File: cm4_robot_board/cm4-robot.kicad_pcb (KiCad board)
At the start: 4 copper layers, 118 x 117 mm, 195 parts, among them J1 1747981-1, J10 Conn_01x04, J11 Conn_01x03, J12 Conn_01x04, J13 CAN Interface, J14 Conn_01x03, J15 Conn_02x04_Odd_Even, J17 Conn_01x04, J18 Conn_01x04, J19 Conn_01x04, J2 CAN Interface, J20 Conn_01x04, J21 Conn_01x03, J22 Conn_01x04, J23 Conn_01x01, J24 Conn_01x01, J25 RJ45, J3 USB_C_Receptacle_USB2.0, J4 Conn_01x04, J5 Conn_01x04, J6 Conn_01x04, J7 USB_A, J8 HIGHCURRENTPAD2, J9 HIGHCURRENTPAD2, Q1 Q_PMOS_GSD, Q2 Q_NMOS_GSD, Q3 Q_NMOS_GSD, Q4 Q_NMOS_GSD, Q5 Q_NMOS_GSD, Q6 AO3401A, Q7 AO3400A, Q8 Si2328DS, SW1 B3U-1000P, SW2 SW_SPDT, SW3 SW_SPDT, SW4 SW_SPDT, U1 SN74LVC1G07QDCKTQ1, U10 isolator, U11 isolator, U12 TPS61040DBVR, U13 SC16IS752, U14 SC16IS752, U15 SN74LVC1G07QDCKTQ1, U16 CC56-12SEKWA, U17 ET6226M, U18 SN74LVC1G07QDCKTQ1, U19 SN74LVC1G07QDCKTQ1, U2 SN74LVC1G07QDCKTQ1, U20 NCP1117-3.3_SOT223, U22 MT2492, U23 TPD4E1U06DCKR, U3 LM2576HVS-5, U4 TPD4E1U06DCKR, U5 ISL54222AIUZ, U6 LTC4412xS6, U7 TXS0101DCKR, U8 MCP2515-xSO, U9 MCP2515-xSO, Y1 16MHz, Y2 16MHz, Y3 14.7456MHz, Y4 14.7456MHz

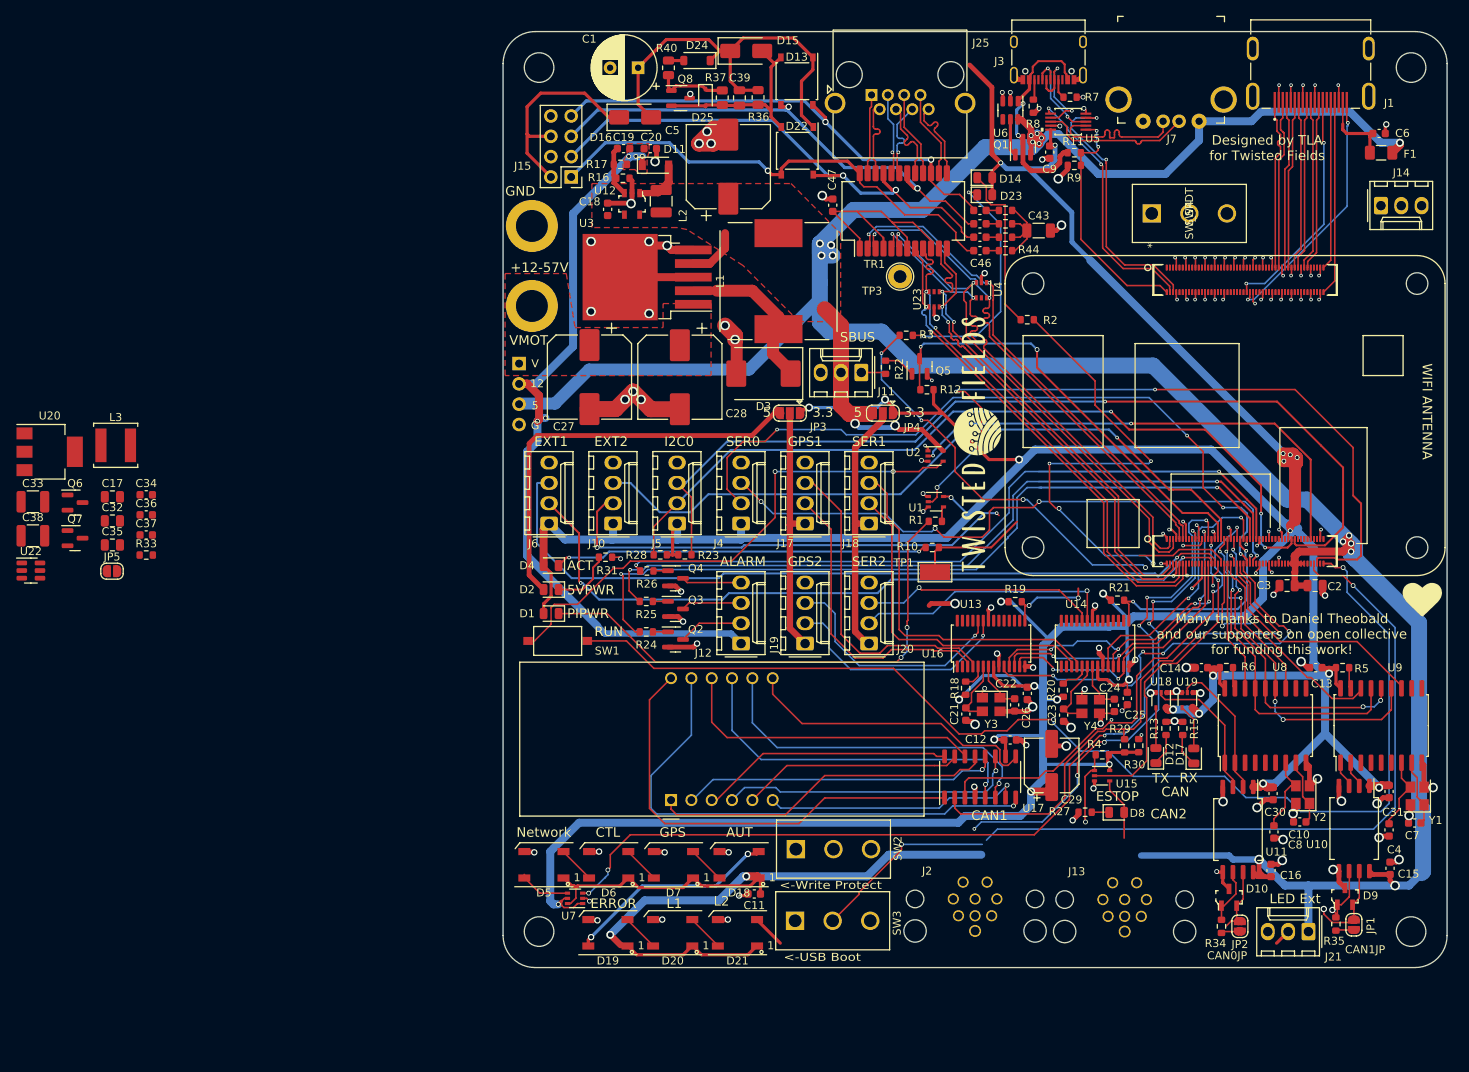
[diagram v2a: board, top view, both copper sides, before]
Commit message: CM4 robot board almost done for Rev 3.5
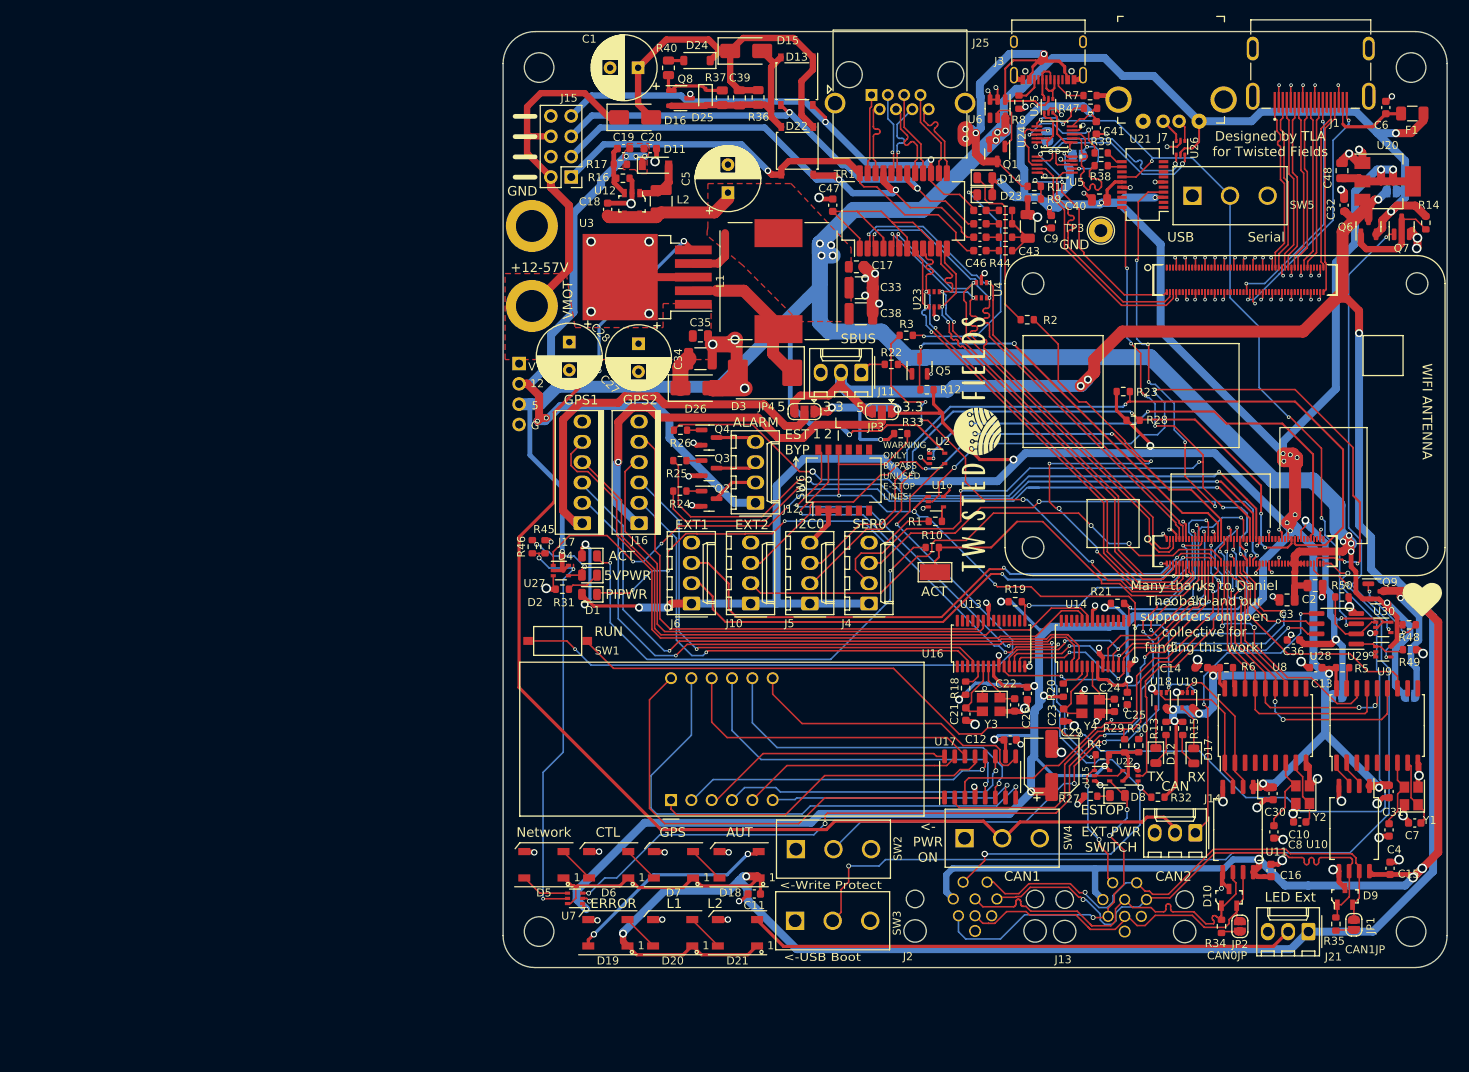
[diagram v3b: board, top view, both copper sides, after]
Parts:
- removed C37: 22uF 6.3v, Capacitor_SMD:C_0603_1608Metric
- removed J18, J19, J20: Conn_01x04, Connector_Molex:Molex_KK-254_AE-6410-04A_1x04_P2.54mm_Vertical
- removed L3: 10uH, Inductor_SMD:L_Sunlord_SWPA5040S
- added C40: 0.1uF, Capacitor_SMD:C_0805_2012Metric, F.Cu at (114.6, 51.0)
- added C41: 0.1uF, Capacitor_SMD:C_0603_1608Metric, F.Cu at (114.2, 42.0)
- added C48: 10u, Capacitor_SMD:C_0805_2012Metric, F.Cu at (144.9, 47.4)
- added D26: SMAJ51A, Diode_SMD:D_SMA, F.Cu at (64.2, 74.6)
- added J16: Encoder 1, parts:Ckmtw-W-2510S06P_1x06_P2.54mm_Vertical, F.Cu at (56.7, 91.4)
- added JP6: SolderJumper_2_Open, Jumper:SolderJumper-2_P1.3mm_Open_RoundedPad1.0x1.5mm, B.Cu at (111.8, 45.5)
- added JP7: SolderJumper_2_Open, Jumper:SolderJumper-2_P1.3mm_Open_RoundedPad1.0x1.5mm, B.Cu at (108.0, 43.1)
- added JP8: SolderJumper_2_Open, Jumper:SolderJumper-2_P1.3mm_Open_RoundedPad1.0x1.5mm, B.Cu at (153.4, 113.0)
- added JP9: SolderJumper_2_Open, Jumper:SolderJumper-2_P1.3mm_Open_RoundedPad1.0x1.5mm, B.Cu at (151.1, 50.0)
- added Q9: AO3401A, Package_TO_SOT_SMD:SOT-23, F.Cu at (149.1, 100.0)
- added R14: 10k, Resistor_SMD:R_0603_1608Metric, F.Cu at (155.3, 53.9)
- added R32: 2.2k 1%, Resistor_SMD:R_0603_1608Metric, F.Cu at (121.9, 125.7)
- added R38: 27, Resistor_SMD:R_0603_1608Metric, F.Cu at (114.8, 46.8)
- added R39: 27, Resistor_SMD:R_0603_1608Metric, F.Cu at (114.8, 45.2)
- added R45: 10k, Resistor_SMD:R_0603_1608Metric, F.Cu at (45.2, 94.4)
- added R46: 5.1k, Resistor_SMD:R_0603_1608Metric, F.Cu at (43.7, 94.4)
- added R47: 10k, Resistor_SMD:R_0603_1608Metric, F.Cu at (113.4, 39.6)
- added R48: 10k, Resistor_SMD:R_0603_1608Metric, F.Cu at (153.3, 104.2)
- added R49: 10k, Resistor_SMD:R_0603_1608Metric, F.Cu at (153.3, 107.3)
- added R50: 10k, Resistor_SMD:R_0603_1608Metric, F.Cu at (144.9, 100.7)
- added SW5: SW_SPDT, parts:CS12ANW03, F.Cu at (126.2, 50.5)
- added SW6: CONFIG SWITCH, Button_Switch_SMD:SW_DIP_SPSTx06_Slide_KingTek_DSHP06TS_W7.62mm_P1.27mm, F.Cu at (82.6, 86.1)
- added U21: FT231XS, Package_SO:SSOP-20_3.9x8.7mm_P0.635mm, F.Cu at (120.0, 49.1)
- added U24: ISL54222AIUZ, parts:ISL54222AIUZ, F.Cu at (108.9, 42.9)
- added U25: USBLC6-2P6, Package_TO_SOT_SMD:SOT-666, F.Cu at (108.2, 39.3)
- added U26: USBLC6-2P6, Package_TO_SOT_SMD:SOT-666, F.Cu at (124.7, 44.5)
- added U27: SN74LVC1G07QDCKTQ1, Package_TO_SOT_SMD:SOT-353_SC-70-5, F.Cu at (47.2, 97.4)
- added U28: PCA9536D, Package_SO:SOIC-8_3.9x4.9mm_P1.27mm, F.Cu at (144.2, 104.7)
- added U29: SN74LVC1G07QDCKTQ1, Package_TO_SOT_SMD:SOT-353_SC-70-5, F.Cu at (150.0, 107.5)
- added U30: SN74LVC1G07QDCKTQ1, Package_TO_SOT_SMD:SOT-353_SC-70-5, F.Cu at (150.0, 104.5)
- C27, C28: value 47uF -> 47uF 63V solid; footprint Capacitor_SMD:CP_Elec_10x10 -> Capacitor_THT:CP_Radial_D8.0mm_P3.50mm
- C32: value 10u -> 1u; footprint Capacitor_SMD:C_0805_2012Metric -> Capacitor_SMD:C_0603_1608Metric
- C34: value 22pF -> 4.7uF 100V; footprint Capacitor_SMD:C_0603_1608Metric -> Capacitor_SMD:C_1210_3225Metric
- C35: value 22uF 10v -> 100nF 100V
- C36: value 22uF 6.3v -> 0.1uF
- C5: value 1000uF -> 1000uF 10v solid; footprint Capacitor_SMD:CP_Elec_10x10 -> Capacitor_THT:CP_Radial_D8.0mm_P3.50mm
- J17: value Conn_01x04 -> Encoder 1; footprint Connector_Molex:Molex_KK-254_AE-6410-04A_1x04_P2.54mm_Vertical -> parts:Ckmtw-W-2510S06P_1x06_P2.54mm_Vertical
- JP5: moved to B.Cu
- R31: value 82R -> 200R
- R33: value 2.2k 1% -> 10k
- R36: value 24.1k/1% -> 24k
- U20: value NCP1117-3.3_SOT223 -> TLV1117LV33DCYR
- U22: value MT2492 -> SN74LVC1G07QDCKTQ1; footprint Package_TO_SOT_SMD:SOT-23-6 -> Package_TO_SOT_SMD:SOT-353_SC-70-5
- moved U20 170.6 mm to (150.6, 48.7)
- moved Q7 170.3 mm to (152.3, 54.4), turned to 90 degrees
- moved Q6 165.3 mm to (148.2, 54.4), turned to 90 degrees
- moved C32 158.9 mm to (145.1, 51.7), turned to 90 degrees
- moved JP5 154.0 mm to (144.3, 113.1), turned to 180 degrees
- moved C36 144.2 mm to (138.8, 106.0), turned to 180 degrees
- moved U22 139.8 mm to (118.4, 123.0), turned to 180 degrees
- moved C38 107.2 mm to (84.7, 65.3)
- moved C33 106.9 mm to (84.7, 62.0)
- moved C17 97.3 mm to (84.2, 59.4)
- moved R33 95.5 mm to (89.7, 80.3)
- moved J14 81.8 mm to (126.5, 130.2), turned to 180 degrees
- moved SW4 81.5 mm to (97.7, 130.8)
- moved C35 78.0 mm to (64.7, 68.1)
- moved C34 71.3 mm to (64.7, 70.9)
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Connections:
- net Net-(Module1A-PI_nLED_Activity) renamed PI_n_LED_ACT
- C11 pad 1: +5V -> 5V_switched
- C15 pad 2: +5V -> 5V_switched_CAN
- C16 pad 2: +5V -> 5V_switched_CAN
- C32 pad 1: +3V3 -> 5V_switched
- C34 pad 1: unconnected-(C34-Pad1) -> VMOT
- C34 pad 2: unconnected-(C34-Pad2) -> GND
- C35 pad 1: +5V -> VMOT
- C36 pad 1: unconnected-(C36-Pad1) -> 3.3V_PI_OUT
- C36 pad 2: unconnected-(C36-Pad2) -> GND
- D1 pad 2: LED_PWR -> +3V3
- D18 pad 1: +5V -> 5V_switched
- D19 pad 1: +5V -> 5V_switched
- D2 pad 2: LED_PWR -> Net-(D2-A)
- D20 pad 1: +5V -> 5V_switched
- D21 pad 1: +5V -> 5V_switched
- D5 pad 1: +5V -> 5V_switched
- D6 pad 1: +5V -> 5V_switched
- D7 pad 1: +5V -> 5V_switched
- J11 pad 2: +5V -> 5V_switched
- J13 pad 1: ESTOP_SINK -> ESTOP_SINK2
- J13 pad 7: 5V_switched -> 5V_switched_CAN
- J14 pad 1: unconnected-(J14-Pin_1-Pad1) -> EXTRA_GPIO
- J17 pad 1: SERIALPWR1 -> SERIALPWR2
- J17 pad 4: GND -> Net-(J17-Pin_4)
- J2 pad 1: ESTOP_SINK -> ESTOP_SINK1
- J2 pad 7: 5V_switched -> 5V_switched_CAN
- J21 pad 1: +5V -> 5V_switched
- JP3 pad 3: +5V -> 5V_switched
- JP4 pad 3: +5V -> 5V_switched
- JP5 pad 1: +3V3 -> 3.3V_PI_OUT
- JP5 pad 2: LED_PWR -> +3V3
- Module1 pad 86: 3.3V_ENABLE -> 3.3V_PI_OUT
- Q7 pad 1: 3.3V_ENABLE -> Net-(Q7-G)
- R13 pad 1: LED_PWR -> +3V3
- R15 pad 1: LED_PWR -> +3V3
- R31 pad 1: Net-(D2-K) -> GND
- R31 pad 2: GND -> Net-(D2-K)
- R33 pad 1: +5V -> +3V3
- R33 pad 2: Net-(Q6-G) -> //LED_EN
- R4 pad 1: ESTOP_SINK -> ESTOP_SINK2
- U1 pad 1: GND -> //LED_EN
- U10 pad 8: +5V -> 5V_switched_CAN
- U11 pad 8: +5V -> 5V_switched_CAN
- U13 pad 3: Net-(J17-Pin_2) -> Net-(J16-Pin_2)
- U13 pad 4: Net-(J17-Pin_3) -> Net-(J16-Pin_3)
- U14 pad 23: Net-(J20-Pin_2) -> Net-(J17-Pin_4)
- U14 pad 24: Net-(J20-Pin_3) -> Net-(J17-Pin_5)
- U14 pad 3: Net-(J18-Pin_2) -> Net-(J17-Pin_2)
- U14 pad 4: Net-(J18-Pin_3) -> Net-(J17-Pin_3)
- U15 pad 1: ESTOP_SINK -> ESTOP_SINK2
- U15 pad 2: ESTOP -> Net-(U15-A)
- U18 pad 1: GND -> //LED_EN
- U19 pad 1: GND -> //LED_EN
- U22 pad 1: unconnected-(U22-BS-Pad1) -> ESTOP_SINK1
- U22 pad 2: GND -> ESTOP
- U22 pad 3: unconnected-(U22-FB-Pad3) -> GND
- U22 pad 4: 3.3V_ENABLE -> Net-(U15-A)
- U22 pad 5: +5V -> +3V3
- U5 pad 2: USBA_D_P -> USBAP_D_P
- U5 pad 3: USBC_D_P -> USB_SW_D+
- U5 pad 7: USBC_D_N -> USB_SW_D-
- U5 pad 8: USBA_D_N -> USBAP_D_N
- U7 pad 5: +3V3 -> /LED_EN_NONINVERTED
- U7 pad 6: +5V -> 5V_switched
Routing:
- net 5V_switched: track 0.00 -> 353.4 mm, vias 0 -> 6
- net /~{5V_EN}: track 0.00 -> 159.0 mm, vias 0 -> 2
- net +5V: track 554.8 -> 407.8 mm, vias 20 -> 16
- net 5V_switched_CAN: track 0.00 -> 137.0 mm, vias 0 -> 4
- net //LED_EN: track 0.00 -> 124.7 mm, vias 0 -> 9
- net +3V3: track 576.4 -> 697.4 mm, vias 27 -> 42
- net ESTOP_SINK1: track 0.00 -> 106.1 mm, vias 0 -> 5
- net SER_SELECT: track 0.00 -> 99.1 mm, vias 0 -> 6
- net Net-(J17-Pin_5): track 0.00 -> 85.6 mm
- net ESTOP_SINK2: track 0.00 -> 83.9 mm, vias 0 -> 6
- net Net-(J17-Pin_4): track 0.00 -> 81.3 mm
- net Net-(D21-DOUT): track 6.15 -> 68.5 mm
- net Net-(J16-Pin_3): track 0.00 -> 59.7 mm, vias 0 -> 1
- net Net-(J16-Pin_2): track 0.00 -> 57.7 mm, vias 0 -> 1
- net Net-(Q7-G): track 0.00 -> 55.7 mm, vias 0 -> 2
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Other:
- board text added: "1"
- board text added: "2"
- board text added: "3.3V"
- board text added: "5V Sw CAN"
- board text added: "5V Switched"
- board text added: "<- PWR ON"
- board text added: "Acorn Motherboard V3.5 This board is open source, please fork it and make it your own! CERN OHL-P License github.com/twisted-fields Love Everyone"
- board text added: "EST BYP"
- board text added: "EXT PWR SWITCH"
- board text added: "Serial"
- board text added: "USB"
- board text added: "WARNING ONLY BYPASS UNUSED E-STOP LINES!"
- board text removed: "Acorn Motherboard V3.0 This board is open source, please fork it and make it your own! CERN OHL-P License github.com/twisted-fields Love Everyone"
- board text removed: "SER1"
- board text removed: "SER2"

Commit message: Updated Motherboard design files to latest version.
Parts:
- removed JP1, JP2: SolderJumper_2_Open, Jumper:SolderJumper-2_P1.3mm_Open_RoundedPad1.0x1.5mm
- added C37: 0.1uF, Capacitor_SMD:C_0603_1608Metric, F.Cu at (124.1, 70.0)
- added C49: 0.1uF, Capacitor_SMD:C_0603_1608Metric, F.Cu at (110.4, 64.5)
- added C50: 0.1uF, Capacitor_SMD:C_0603_1608Metric, F.Cu at (111.9, 68.9)
- added C51: 1u, Capacitor_SMD:C_0603_1608Metric, F.Cu at (111.9, 66.9)
- added JP10: SolderJumper_2_Open, Jumper:SolderJumper-2_P1.3mm_Open_RoundedPad1.0x1.5mm, F.Cu at (130.7, 70.9)
- added R51: 5.1k, Resistor_SMD:R_0603_1608Metric, F.Cu at (127.3, 69.1)
- added R52: 5.1k, Resistor_SMD:R_0603_1608Metric, F.Cu at (115.1, 65.4)
- added SW7: CONFIG_SW, Button_Switch_SMD:SW_DIP_SPSTx04_Slide_KingTek_DSHP04TS_W7.62mm_P1.27mm, F.Cu at (81.2, 86.0)
- added TP2: TestPoint, TestPoint:TestPoint_Loop_D2.60mm_Drill1.6mm_Beaded, F.Cu at (43.2, 87.4)
- added U31: LSM6DS3, Package_LGA:LGA-14_3x2.5mm_P0.5mm_LayoutBorder3x4y, F.Cu at (125.5, 72.6)
- added U32: LIS3MDL, Package_LGA:LGA-12_2x2mm_P0.5mm, F.Cu at (112.8, 64.4)
- J16, J17: value Encoder 1 -> ~
- SW6: value CONFIG SWITCH -> SW_DIP_x02; footprint Button_Switch_SMD:SW_DIP_SPSTx06_Slide_KingTek_DSHP06TS_W7.62mm_P1.27mm -> Button_Switch_SMD:SW_DIP_SPSTx02_Slide_KingTek_DSHP02TS_W7.62mm_P1.27mm
- moved SW6 76.1 mm to (135.2, 141.1)
- moved D26 26.3 mm to (52.2, 51.1), turned to 90 degrees
- moved C18 6.94 mm to (59.9, 53.3), turned to 180 degrees
- moved D9 6.58 mm to (141.1, 133.0), turned to 180 degrees
- moved J21 5.96 mm to (145.5, 139.0), turned to -90 degrees
- moved R35 5.50 mm to (138.6, 141.7)
- moved U12 3.58 mm to (59.3, 49.9)
- moved L2 3.38 mm to (63.0, 50.1)
- moved D11 2.93 mm to (61.6, 45.2), turned to -90 degrees
- moved R17 2.88 mm to (57.5, 46.1), turned to 90 degrees
- moved R16 1.93 mm to (56.7, 49.3), turned to 90 degrees
- moved C20 1.79 mm to (59.3, 46.2), turned to -90 degrees
- moved C19 1.74 mm to (55.9, 46.1), turned to -90 degrees
- moved R2 1.28 mm to (104.7, 67.0)
- moved C5 1.00 mm to (69.1, 50.1)
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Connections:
- net 3.3V_PI_CONTROL renamed 3.3V_5V_PI_CONTROL
- net CAN_SCS0 renamed CAN_CS0
- net CAN_SCS1 renamed CAN_CS1
- net CAN_SI renamed CAN_COPI
- net CAN_SO renamed CAN_CIPO
- net SERIAL_SI renamed SERIAL_CIPO
- net SERIAL_SO renamed SERIAL_COPI
- R34 pad 2: Net-(JP2-B) -> Net-(R34-Pad2)
- R35 pad 2: Net-(JP1-B) -> Net-(R35-Pad2)
- SW6 pad 1: GND -> Net-(R34-Pad2)
- SW6 pad 2: GND -> Net-(R35-Pad2)
- SW6 pad 3: GND -> /CAN1_P
- SW6 pad 4: unconnected-(SW6-Pad4) -> /CAN0_P
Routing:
- net SCL6: track 72.8 -> 127.4 mm, vias 2 -> 7
- net +3V3: track 697.4 -> 749.1 mm, vias 42 -> 45
- net SDA6: track 84.1 -> 135.0 mm, vias 6 -> 11
- net GND: track 267.7 -> 296.5 mm, vias 156 -> 170
- net Net-(D21-DOUT): track 68.5 -> 77.6 mm
- net FB: track 6.43 -> 0.00 mm
- net Net-(D11-A): track 6.36 -> 0.00 mm
- net Net-(JP10-B): track 0.00 -> 5.94 mm
- net Net-(R34-Pad2): track 0.00 -> 5.71 mm
- net Net-(R35-Pad2): track 0.00 -> 3.73 mm
- net VMOT: track 49.7 -> 46.4 mm
- net +5V: track 407.8 -> 410.9 mm, vias 16 -> 18
- net /~{5V_EN}: track 159.0 -> 161.5 mm
- net Net-(JP2-B): track 2.37 -> 0.00 mm
- net Net-(JP1-B): track 2.29 -> 0.00 mm
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- added copper zone on F.Cu, net FB
- added copper zone on F.Cu, net GND
- added copper zone on F.Cu, net Net-(D11-A)
